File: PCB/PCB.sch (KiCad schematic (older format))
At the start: 124 parts, among them J1 AudioJack3, J10 Conn_01x02, J11 Conn_01x01, J12 Conn_01x02, J13 Conn_01x01, J14 Conn_01x01, J15 Conn_01x01, J16 Conn_01x01, J17 Conn_01x01, J18 Conn_01x01, J2 Conn, J3 Screw_Terminal_01x02, J4 Screw_Terminal_01x02, J5 Screw_Terminal_01x02, J6 Screw_Terminal_01x02, J7 REALIMENTACION, J8 Conn_01x02, J9 Conn_01x02, Q1 MMBTA06, Q10 MMBTA06, Q11 MMBTA56, Q12 MMBTA06, Q13 MMBTA56, Q14 MMBTA56, Q15 MMBTA56, Q16 MMBTA06, Q17 MMBTA06, Q18 MMBTA06, Q19 MMBTA56, Q2 MMBTA56, Q20 MMBTA06, Q21 MMBTA56, Q22 Q-NPN, Q23 2SA1943, Q24 MJE350, Q25 MJE340, Q26 2SC5200, Q27 2SA1943, Q28 MMBTA06, Q29 MMBTA56, Q3 Q_NPN_BCE, Q4 MMBTA56, Q5 MMBTA06, Q6 MMBTA56, Q7 MMBTA56, Q8 MJE340, Q9 MMBTA06

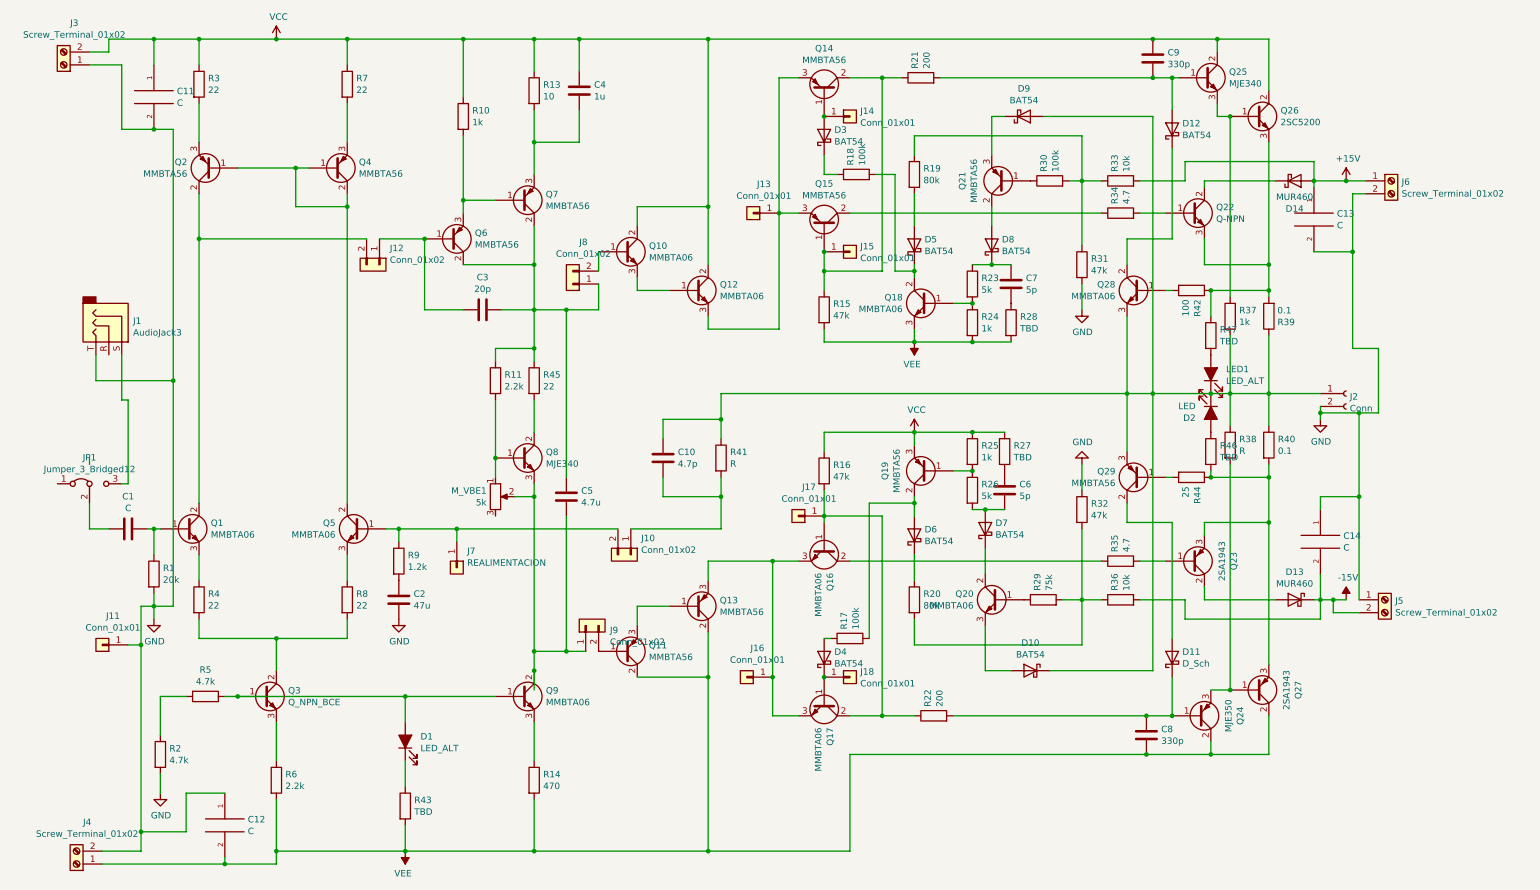
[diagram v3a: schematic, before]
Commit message: Added resistors for miniplugs. Added name to pcb. Small modifications
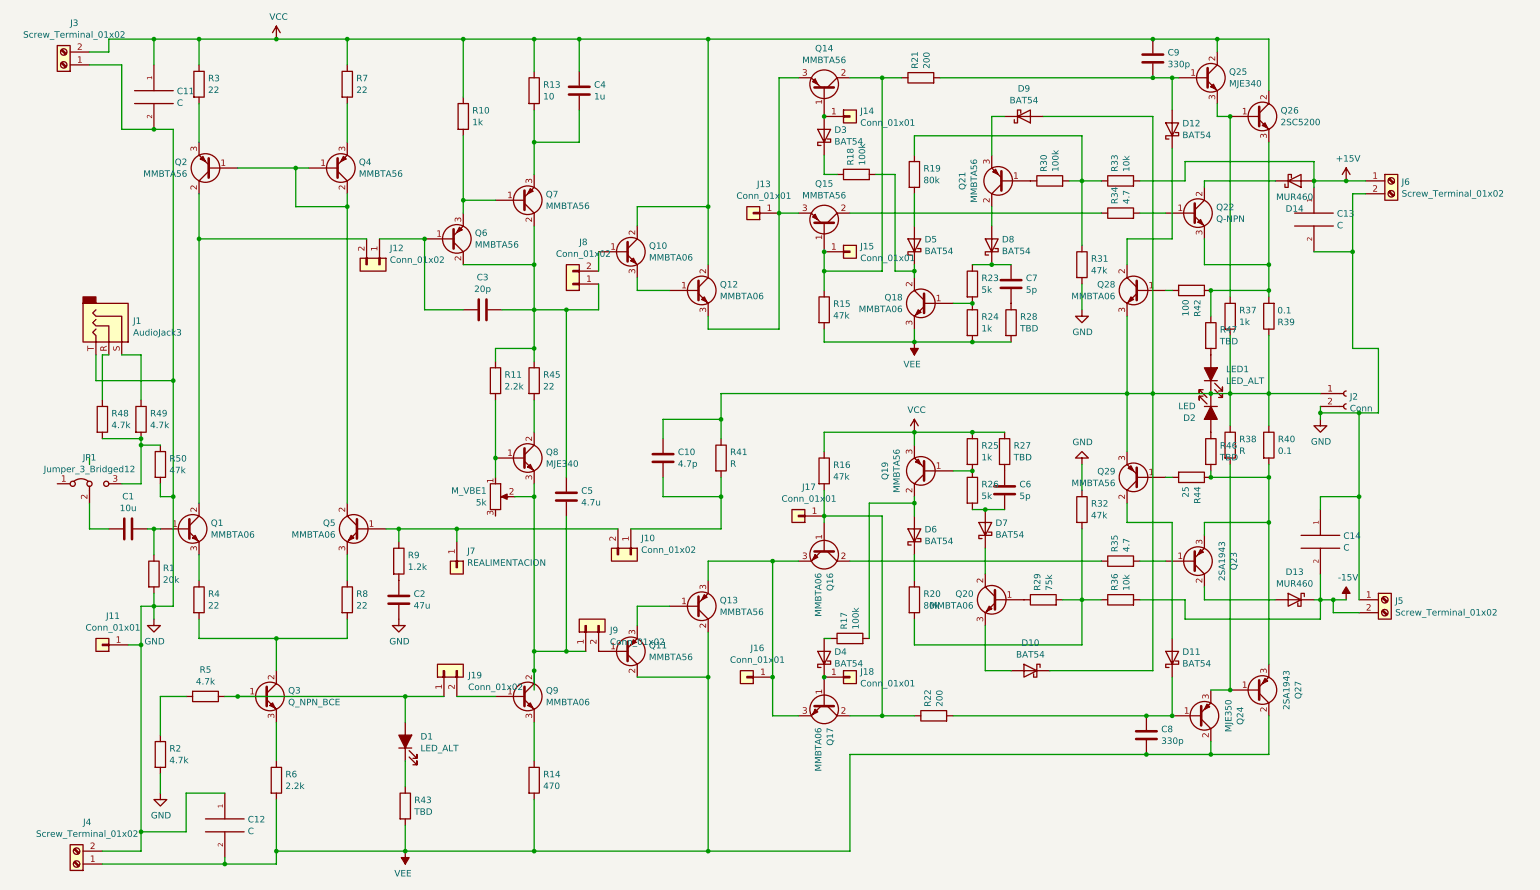
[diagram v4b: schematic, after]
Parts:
- added J19: Conn_01x02, Connector_PinHeader_2.54mm:PinHeader_1x02_P2.54mm_Vertical, symbol Connector_Generic:Conn_01x02
- added R48, R49: 4.7k, Resistor_SMD:R_1206_3216Metric_Pad1.30x1.75mm_HandSolder, symbol Device:R
- added R50: 47k, Resistor_SMD:R_1206_3216Metric_Pad1.30x1.75mm_HandSolder, symbol Device:R
- C1: value C -> 10u
- D11: value D_Sch -> BAT54
- J1: footprint Connector:PJ320D_3.5mm_Jack -> Connector_Audio:Jack_3.5mm_CUI_SJ-3523-SMT_Horizontal
- JP1: footprint Connector:Fan_Pin_Header_Straight_1x03 -> Connector_PinHeader_2.54mm:PinHeader_1x03_P2.54mm_Vertical
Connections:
- net GND: now also R50.2
- net at D1.2 (A), Q3.1 (B), R5.1: now also J19.1 (Pin_1); no longer Q9.1 (B)
- net at JP1.3 (B): now also R48.2, R49.2, R50.1; no longer J1.S
- net at J1.R: now also R48.1
- new net: J19.2 (Pin_2), Q9.1 (B)
- new net: J1.S, R49.1
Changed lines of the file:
@@
 P 1100 4550
 F 0 "C1" V 1352 4550 50  0000 C CNN
-F 1 "C" V 1261 4550 50  0000 C CNN
+F 1 "10u" V 1261 4550 50  0000 C CNN
 F 2 "Capacitor_THT:CP_Radial_D5.0mm_P2.50mm" H 1138 4400 50  0001 C CNN
 F 3 "~" H 1100 4550 50  0001 C CNN
@@
 $EndComp
 Wire Wire Line
-	3250 5850 3950 5850
+	3250 5850 3550 5850
 Wire Wire Line
 	3250 7050 4250 7050
@@
 P 9200 5550
 F 0 "D11" V 9246 5471 50  0000 R CNN
-F 1 "D_Sch" V 9155 5471 50  0000 R CNN
+F 1 "BAT54" V 9155 5471 50  0000 R CNN
 F 2 "Diode_SMD:D_SOT-23_ANK" H 9200 5550 50  0001 C CNN
 F 3 "~" H 9200 5550 50  0001 C CNN
@@
 	1300 5150 1450 5150
 Wire Wire Line
-	1450 5150 1450 3400
+	1450 5150 1450 4300
 Wire Wire Line
 	1450 1450 1300 1450
@@
 F 0 "JP1" H 800 4404 50  0000 C CNN
 F 1 "Jumper_3_Bridged12" H 800 4313 50  0000 C CNN
-F 2 "Connector:Fan_Pin_Header_Straight_1x03" H 800 4200 50  0001 C CNN
+F 2 "Connector_PinHeader_2.54mm:PinHeader_1x03_P2.54mm_Vertical" H 800 4200 50  0001 C CNN
 F 3 "~" H 800 4200 50  0001 C CNN
 	1    800  4200
@@
 Wire Wire Line
 	800  4000 800  4050
-Wire Wire Line
-	1050 4200 1100 4200
 Wire Wire Line
 	800  4350 800  4550
@@
 F 0 "J1" V 886 3188 50  0000 L CNN
 F 1 "AudioJack3" V 977 3188 50  0000 L CNN
-F 2 "Connector:PJ320D_3.5mm_Jack" H 950 3000 50  0001 C CNN
+F 2 "Connector_Audio:Jack_3.5mm_CUI_SJ-3523-SMT_Horizontal" H 950 3000 50  0001 C CNN
 F 3 "~" H 950 3000 50  0001 C CNN
 	1    950  3000
@@
 $EndComp
 Wire Wire Line
-	1050 3200 1050 3550
-Wire Wire Line
-	1050 3550 1100 3550
-Wire Wire Line
 	850  3200 850  3400
 Wire Wire Line
@@
 Wire Wire Line
 	1450 3400 1450 1450
-Wire Wire Line
-	1100 3550 1100 4200
 $Comp
 L Device:R_POT M_VBE1
@@
 $EndComp
 Connection ~ 6500 5700
+$Comp
+L Connector_Generic:Conn_01x02 J19
+U 1 1 60433C35
+P 3550 5650
+F 0 "J19" V 3514 5462 50  0000 R CNN
+F 1 "Conn_01x02" V 3423 5462 50  0000 R CNN
+F 2 "Connector_PinHeader_2.54mm:PinHeader_1x02_P2.54mm_Vertical" H 3550 5650 50  0001 C CNN
+F 3 "~" H 3550 5650 50  0001 C CNN
+	1    3550 5650
+	0    -1   -1   0
+$EndComp
+Wire Wire Line
+	3650 5850 3950 5850
+$Comp
+L Device:R R48
+U 1 1 6048C1CE
+P 900 3700
+F 0 "R48" H 970 3746 50  0000 L CNN
+F 1 "4.7k" H 970 3655 50  0000 L CNN
+F 2 "Resistor_SMD:R_1206_3216Metric_Pad1.30x1.75mm_HandSolder" V 830 3700 50  0001 C CNN
+F 3 "~" H 900 3700 50  0001 C CNN
+	1    900  3700
+	1    0    0    -1
+$EndComp
+$Comp
+L Device:R R49
+U 1 1 6048D0B5
+P 1200 3700
+F 0 "R49" H 1270 3746 50  0000 L CNN
+F 1 "4.7k" H 1270 3655 50  0000 L CNN
+F 2 "Resistor_SMD:R_1206_3216Metric_Pad1.30x1.75mm_HandSolder" V 1130 3700 50  0001 C CNN
+F 3 "~" H 1200 3700 50  0001 C CNN
+	1    1200 3700
+	1    0    0    -1
+$EndComp
+Wire Wire Line
+	900  3550 900  3200
+Wire Wire Line
+	900  3200 950  3200
+Wire Wire Line
+	1050 3200 1200 3200
+Wire Wire Line
+	1200 3200 1200 3550
+Wire Wire Line
+	900  3850 1200 3850
+Wire Wire Line
+	1200 3850 1200 3900
+Wire Wire Line
+	1050 4200 1200 4200
+Connection ~ 1200 3850
+$Comp
+L Device:R R50
+U 1 1 604FC014
+P 1350 4050
+F 0 "R50" H 1420 4096 50  0000 L CNN
+F 1 "47k" H 1420 4005 50  0000 L CNN
+F 2 "Resistor_SMD:R_1206_3216Metric_Pad1.30x1.75mm_HandSolder" V 1280 4050 50  0001 C CNN
+F 3 "~" H 1350 4050 50  0001 C CNN
+	1    1350 4050
+	1    0    0    -1
+$EndComp
+Wire Wire Line
+	1200 3900 1350 3900
+Connection ~ 1200 3900
+Wire Wire Line
+	1200 3900 1200 4200
+Wire Wire Line
+	1350 4200 1350 4300
+Wire Wire Line
+	1350 4300 1450 4300
+Connection ~ 1450 4300
+Wire Wire Line
+	1450 4300 1450 3400
 $EndSCHEMATC
